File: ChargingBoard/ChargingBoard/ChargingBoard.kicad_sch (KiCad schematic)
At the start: 0 parts

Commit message: Integration
Added charging circuits to project schematic, deleted redundant schematics
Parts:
- added BT1, BT2, BT3, BT4: Battery, Battery:BatteryHolder_Keystone_1060_1x2032, symbol Device:Battery
- added C1, C11, C16, C6: 0.1u, Capacitor_SMD:C_0201_0603Metric_Pad0.64x0.40mm_HandSolder, symbol Device:C
- added C10, C15, C20, C5: 10u, symbol Device:C_Polarized
- added C12, C17, C2, C7: 33n, Capacitor_SMD:C_0201_0603Metric_Pad0.64x0.40mm_HandSolder, symbol Device:C
- added C13, C18, C3, C8: 22n, Capacitor_SMD:C_0201_0603Metric_Pad0.64x0.40mm_HandSolder, symbol Device:C
- added C14, C19, C4, C9: 10u, Capacitor_SMD:C_0201_0603Metric_Pad0.64x0.40mm_HandSolder, symbol Device:C
- added D1, D14, D19, D9: GRN, LED_SMD:LED_0201_0603Metric_Pad0.64x0.40mm_HandSolder, symbol Device:LED
- added D10, D15, D20, D5: 6V, Diode_THT:D_DO-41_SOD81_P10.16mm_Horizontal, symbol Diode:1N47xxA
- added D11, D16, D3, D6: BLU, LED_SMD:LED_0201_0603Metric_Pad0.64x0.40mm_HandSolder, symbol Device:LED
- added D12, D17, D2, D7: YEL, LED_SMD:LED_0201_0603Metric_Pad0.64x0.40mm_HandSolder, symbol Device:LED
- added D13, D18, D4, D8: RED, LED_SMD:LED_0201_0603Metric_Pad0.64x0.40mm_HandSolder, symbol Device:LED
- added L1, L2, L3, L4: 6.8u, Inductor_SMD:L_0201_0603Metric_Pad0.64x0.40mm_HandSolder, symbol Device:L
- added Q1, Q10, Q11, Q13, Q14, Q15, Q2, Q3, Q5, Q6, Q7, Q9: FQP27P06, Package_TO_SOT_THT:TO-220-3_Vertical, symbol Transistor_FET:FQP27P06
- added Q12, Q16, Q4, Q8: IRLZ44N, Package_TO_SOT_THT:TO-220-3_Vertical, symbol Transistor_FET:IRLZ44N
- added R1, R20, R21, R33, R34, R46, R47, R7: 10k, Resistor_SMD:R_0201_0603Metric_Pad0.64x0.40mm_HandSolder, symbol Device:R
- added R10, R26, R39, R52: 9.76k, Resistor_SMD:R_0201_0603Metric_Pad0.64x0.40mm_HandSolder, symbol Device:R
- added R11, R19, R32, R45: 100k, Resistor_SMD:R_0201_0603Metric_Pad0.64x0.40mm_HandSolder, symbol Device:R
- added R12, R24, R37, R50: 51k, Resistor_SMD:R_0201_0603Metric_Pad0.64x0.40mm_HandSolder, symbol Device:R
- added R13, R23, R36, R49: 100m, Resistor_SMD:R_0201_0603Metric_Pad0.64x0.40mm_HandSolder, symbol Device:R
- added R14, R15, R17, R18, R27, R28, R3, R30, R31, R4, R40, R41, R43, R44, R5, R6: 3k, Resistor_SMD:R_0201_0603Metric_Pad0.64x0.40mm_HandSolder, symbol Device:R
- added R16, R29, R42, R8: 20k, Resistor_SMD:R_0201_0603Metric_Pad0.64x0.40mm_HandSolder, symbol Device:R
- added R2, R22: 150k, Resistor_SMD:R_0201_0603Metric_Pad0.64x0.40mm_HandSolder, symbol Device:R
- added R25, R38, R51, R9: 28k, Resistor_SMD:R_0201_0603Metric_Pad0.64x0.40mm_HandSolder, symbol Device:R
- added R35, R48: 70k, Resistor_SMD:R_0201_0603Metric_Pad0.64x0.40mm_HandSolder, symbol Device:R
- added TH1, TH2, TH3, TH4: 10k, Resistor_SMD:R_0508_1220Metric_Pad1.12x2.15mm_HandSolder, symbol Device:Thermistor_NTC
- added U1, U2, U4, U5: LTC4011CFE, Package_SO:HTSSOP-20-1EP_4.4x6.5mm_P0.65mm_EP2.74x3.86mm, symbol Battery_Management:LTC4011CFE
- added U3: ATmega328-P, Package_DIP:DIP-28_W7.62mm, symbol MCU_Microchip_ATmega:ATmega328-P
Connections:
- new net: R1.1, U1.9 (V_{CDIV})
- new net: C2.1, R1.2, R2.2, U1.8 (V_{CELL})
- new net: D20.2 (A), Q14.1 (G), R47.1
- new net: R10.2, R12.2, R9.1, TH1.1
- new net: D13.1 (K), U4.2 (~{FAULT})
- new net: D13.2 (A), R30.2
- new net: R45.2, U5.10 (TIMER)
- new net: D10.2 (A), Q6.1 (G), R21.1
- new net: R24.2, R25.1, R26.2, TH2.1
- new net: R37.2, R38.1, R39.2, TH3.1
- new net: C6.1, U2.14 (INTVDD)
- new net: C7.1, R20.2, R22.2, U2.8 (V_{CELL})
- new net: R19.2, U2.10 (TIMER)
- new net: D15.2 (A), Q10.1 (G), R34.1
- new net: C1.1, U1.14 (INTVDD)
- new net: R50.2, R51.1, R52.2, TH4.1
- new net: C12.1, R33.2, R35.2, U4.8 (V_{CELL})
- new net: D12.2 (A), R28.2
- new net: D6.2 (A), R14.2
- new net: D11.2 (A), R27.2
- new net: D14.2 (A), R31.2
- new net: R32.2, U4.10 (TIMER)
- new net: L3.2, R36.1, U4.11 (SENSE)
- new net: D12.1 (K), U4.13 (~{TOC})
- new net: C11.1, U4.14 (INTVDD)
- new net: D14.1 (K), U4.19 (~{READY})
- new net: D11.1 (K), U4.3 (~{CHRG})
- new net: R33.1, U4.9 (V_{CDIV})
- new net: D18.2 (A), R43.2
- new net: D1.1 (K), U1.19 (~{READY})
- new net: D1.2 (A), R3.2
- new net: R11.2, U1.10 (TIMER)
- new net: L1.2, R13.1, U1.11 (SENSE)
- new net: D7.2 (A), R15.2
- new net: C17.1, R46.2, R48.2, U5.8 (V_{CELL})
- new net: R20.1, U2.9 (V_{CDIV})
- new net: D8.1 (K), U2.2 (~{FAULT})
- new net: D8.2 (A), R17.2
- new net: D4.2 (A), R6.2
- new net: D4.1 (K), U1.2 (~{FAULT})
- new net: C16.1, U5.14 (INTVDD)
- new net: L4.2, R49.1, U5.11 (SENSE)
- new net: D6.1 (K), U2.3 (~{CHRG})
- new net: U3.22 (GND), U3.8 (GND)
- new net: D16.2 (A), R40.2
- new net: D3.2 (A), R5.2
- new net: D2.2 (A), R4.2
- new net: D5.2 (A), Q2.1 (G), R7.1
- new net: D3.1 (K), U1.3 (~{CHRG})
- new net: D9.1 (K), U2.19 (~{READY})
- new net: D9.2 (A), R18.2
- new net: L2.2, R23.1, U2.11 (SENSE)
- new net: D17.2 (A), R41.2
- new net: D17.1 (K), U5.13 (~{TOC})
- new net: D7.1 (K), U2.13 (~{TOC})
- new net: D19.1 (K), U5.19 (~{READY})
- new net: D18.1 (K), U5.2 (~{FAULT})
- new net: D16.1 (K), U5.3 (~{CHRG})
- new net: R46.1, U5.9 (V_{CDIV})
- new net: D19.2 (A), R44.2
- new net: D2.1 (K), U1.13 (~{TOC})
- new net +12V: Q13.3 (S), Q5.3 (S)
- new net +18V: C15.1, C20.1, D15.1 (K), D20.1 (K), Q10.3 (S), Q11.3 (S), Q13.2 (D), Q14.3 (S), Q15.3 (S), Q9.2 (D), Q9.3 (S), R27.1, R28.1, R29.2, R30.1, R31.1, R34.2, R40.1, R41.1, R42.2, R43.1, R44.1, R47.2, U4.1 (DCIN), U4.18 (V_{CC}), U5.1 (DCIN), U5.18 (V_{CC})
- new net +34V: C10.1, C5.1, D10.1 (K), D5.1 (K), Q1.2 (D), Q1.3 (S), Q2.3 (S), Q3.3 (S), Q5.2 (D), Q6.3 (S), Q7.3 (S), R14.1, R15.1, R16.2, R17.1, R18.1, R21.2, R3.1, R4.1, R5.1, R6.1, R7.2, R8.2, U1.1 (DCIN), U1.18 (V_{CC}), U2.1 (DCIN), U2.18 (V_{CC})
- new net BAT1: BT1.1 (+), C4.1, Q2.2 (D), R13.2, R2.1, R48.1, U1.12 (BAT), U5.12 (BAT)
- new net BAT2: BT2.1 (+), C9.1, Q6.2 (D), R22.1, R23.2, U2.12 (BAT)
- new net BAT3: BT3.1 (+), C14.1, Q10.2 (D), R35.1, R36.2, U4.12 (BAT)
- new net BAT4: BT4.1 (+), C19.1, Q14.2 (D), R49.2
- new net BGATE1: Q4.1 (G), U1.15 (BGATE)
- new net BGATE2: Q8.1 (G), U2.15 (BGATE)
- new net BGATE3: Q12.1 (G), U4.15 (BGATE)
- new net BGATE4: Q16.1 (G), U5.15 (BGATE)
- new net GND: BT1.2 (-), BT2.2 (-), BT3.2 (-), BT4.2 (-), C1.2, C10.2, C11.2, C12.2, C13.2, C14.2, C15.2, C16.2, C17.2, C18.2, C19.2, C2.2, C20.2, C3.2, C4.2, C5.2, C6.2, C7.2, C8.2, C9.2, Q12.3 (S), Q16.3 (S), Q4.3 (S), Q8.3 (S), R11.1, R16.1, R19.1, R25.2, R29.1, R32.1, R38.2, R42.1, R45.1, R51.2, R8.1, R9.2, TH1.2, TH2.2, TH3.2, TH4.2, U1.16 (PGND), U1.21 (GND), U1.4 (CHEM), U1.5 (GND), U2.16 (PGND), U2.21 (GND), U2.4 (CHEM), U2.5 (GND), U4.16 (PGND), U4.21 (GND), U4.4 (CHEM), U4.5 (GND), U5.16 (PGND), U5.21 (GND), U5.4 (CHEM), U5.5 (GND)
- new net INFET1: Q1.1 (G), U1.20 (INFET)
- new net INFET2: Q5.1 (G), U2.20 (INFET)
- new net INFET3: Q9.1 (G), U4.20 (INFET)
- new net INFET4: Q13.1 (G), U5.20 (INFET)
- new net L1: L1.1, Q3.2 (D), Q4.2 (D)
- new net L2: L2.1, Q7.2 (D), Q8.2 (D)
- new net L3: L3.1, Q11.2 (D), Q12.2 (D)
- new net L4: L4.1, Q15.2 (D), Q16.2 (D)
- new net TGATE1: Q3.1 (G), U1.17 (TGATE)
- new net TGATE2: Q7.1 (G), U2.17 (TGATE)
- new net TGATE3: Q11.1 (G), U4.17 (TGATE)
- new net TGATE4: Q15.1 (G), U5.17 (TGATE)
- new net VRT1: R10.1, U1.6 (V_{RT})
- new net VRT2: R26.1, U2.6 (V_{RT})
- new net VRT3: R39.1, U4.6 (V_{RT})
- new net VRT4: R52.1, U5.6 (V_{RT})
- new net VTEMP1: C3.1, R12.1, U1.7 (V_{TEMP})
- new net VTEMP2: C8.1, R24.1, U2.7 (V_{TEMP})
- new net VTEMP3: C13.1, R37.1, U4.7 (V_{TEMP})
- new net VTEMP4: C18.1, R50.1, U5.7 (V_{TEMP})
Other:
- note added: "MOTOR_1"
- note added: "MOTOR_2"
- note added: "PCB_1"
- note added: "PCB_2"
- company: (none) -> Aurelia
- title: (none) -> MUSTV UOP Charging Board

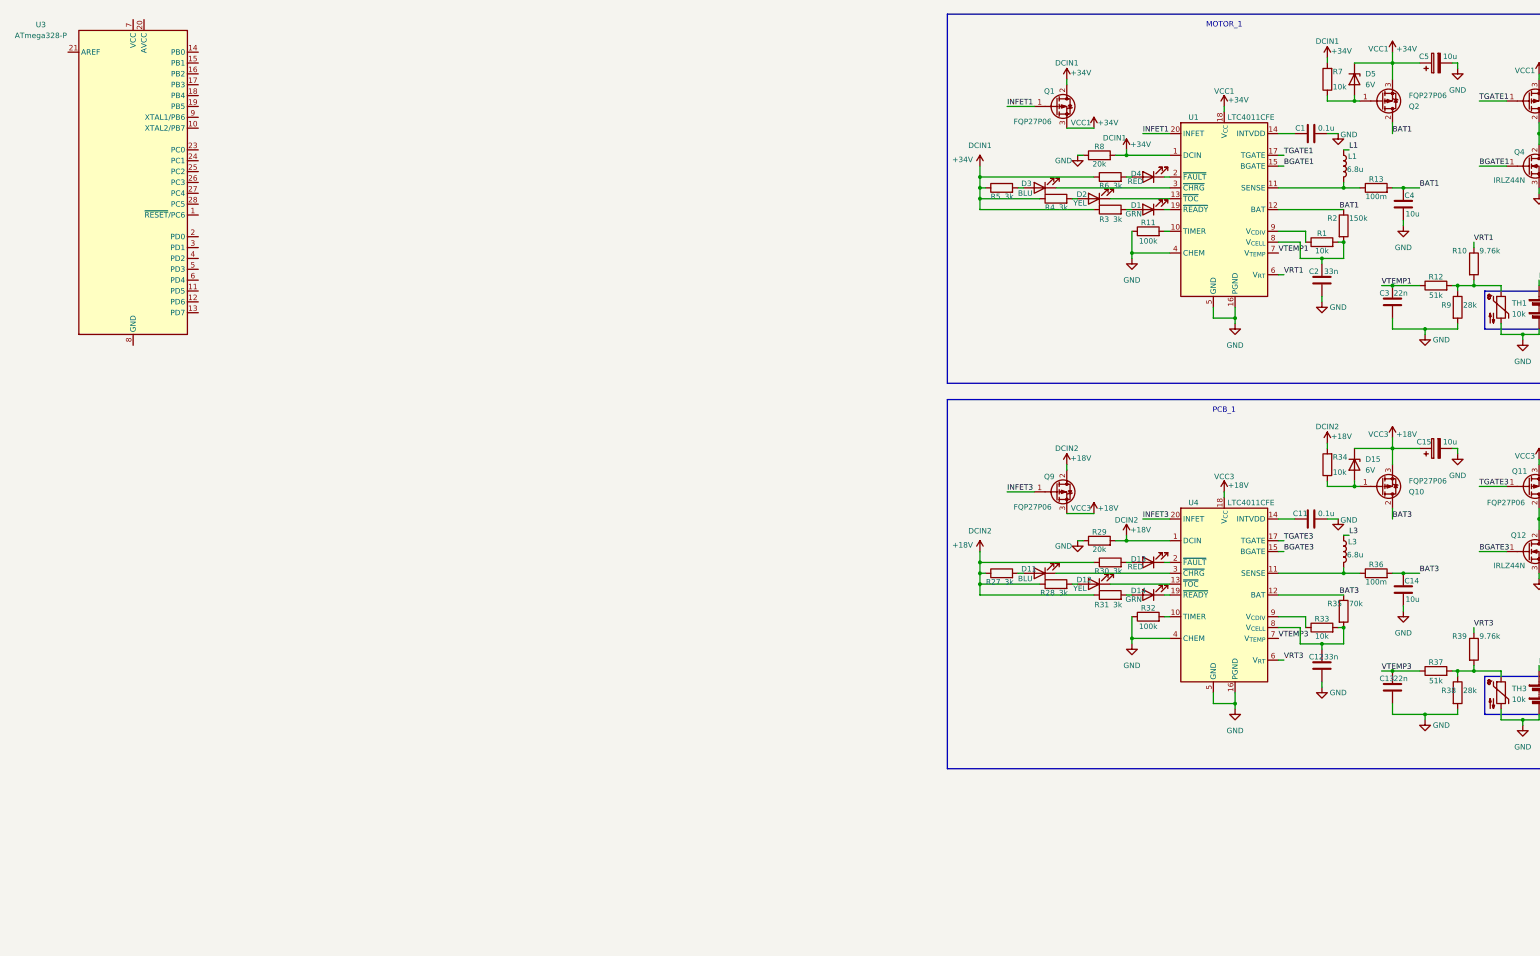
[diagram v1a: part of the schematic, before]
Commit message: SD Card and Voltage Conversion
Swapped out microcontroller, added SD card circuit and conversion terminals for voltages, added 5V to 3.3V regulator
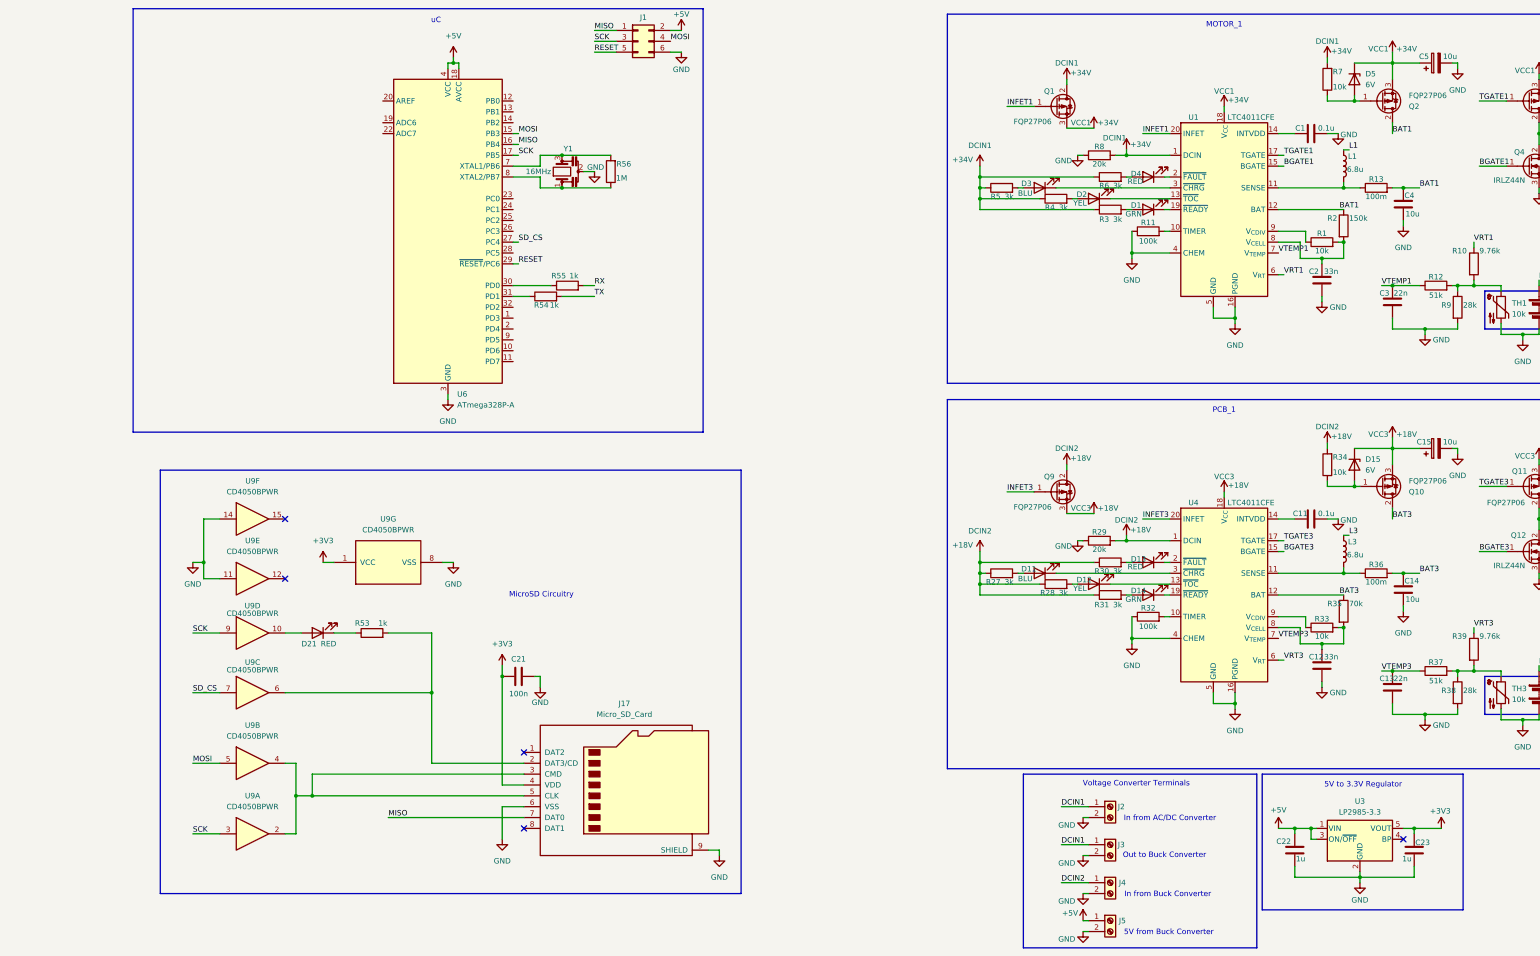
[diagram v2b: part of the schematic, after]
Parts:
- removed U3: ATmega328-P, Package_DIP:DIP-28_W7.62mm, symbol MCU_Microchip_ATmega:ATmega328-P
- added C21: 100n, Capacitor_SMD:C_0603_1608Metric_Pad1.08x0.95mm_HandSolder, symbol Device:C
- added C22, C23: 1u, Capacitor_SMD:C_0603_1608Metric_Pad1.08x0.95mm_HandSolder, symbol Device:C
- added D21: RED, LED_SMD:LED_0603_1608Metric_Pad1.05x0.95mm_HandSolder, symbol Device:LED
- added J1: Conn_02x03_Odd_Even, symbol Connector_Generic:Conn_02x03_Odd_Even
- added J17: Micro_SD_Card, Connector_Card:microSD_HC_Hirose_DM3BT-DSF-PEJS, symbol Connector:Micro_SD_Card
- added J2, J3, J4, J5: Screw_Terminal_01x02, symbol Connector:Screw_Terminal_01x02
- added R53: 1k, Resistor_SMD:R_0603_1608Metric_Pad0.98x0.95mm_HandSolder, symbol Device:R
- added R54, R55: 1k, symbol Device:R
- added R56: 1M, symbol Device:R
- added U3: LP2985-3.3, Package_TO_SOT_SMD:SOT-23-5_HandSoldering, symbol Regulator_Linear:LP2985-3.3
- added U6: ATmega328P-A, Package_QFP:TQFP-32_7x7mm_P0.8mm, symbol MCU_Microchip_ATmega:ATmega328P-A
- added U9: CD4050BPWR, Package_SO:SOIC-16_3.9x9.9mm_P1.27mm, symbol 4xxx:4050
- added Y1: 16MHz, symbol Device:Resonator
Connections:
- net GND: now also C21.2, C22.2, C23.2, J1.6 (Pin_6), J17.6 (VSS), J17.9 (SHIELD), J2.2 (Pin_2), J3.2 (Pin_2), J4.2 (Pin_2), J5.2 (Pin_2), U3.2 (GND), U6.21 (GND), U6.3 (GND), U6.5 (GND), U9.11, U9.14, U9.8 (VSS), Y1.2
- new net: R56.1, U6.8 (XTAL2/PB7), Y1.1
- new net: R56.2, U6.7 (XTAL1/PB6), Y1.3
- new net: J17.3 (CMD), J17.5 (CLK), U9.2, U9.4
- new net: D21.1 (K), R53.1
- new net: J17.2 (DAT3/CD), R53.2, U9.6
- new net: D21.2 (A), U9.10
- new net: R55.1, U6.30 (PD0)
- new net: R54.1, U6.31 (PD1)
- new net +3V3: C21.1, C23.1, J17.4 (VDD), U3.5 (VOUT), U9.1 (VCC)
- new net +5V: C22.1, J1.2 (Pin_2), J5.1 (Pin_1), U3.1 (VIN), U3.3 (ON/~{OFF}), U6.18 (AVCC), U6.4 (VCC), U6.6 (VCC)
- new net DCIN1: J2.1 (Pin_1), J3.1 (Pin_1)
- new net DCIN2: J4.1 (Pin_1)
- new net MISO: J1.1 (Pin_1), J17.7 (DAT0), U6.16 (PB4)
- new net MOSI: J1.4 (Pin_4), U6.15 (PB3), U9.5
- new net RESET: J1.5 (Pin_5), U6.29 (~{RESET}/PC6)
- new net RX: R55.2
- new net SCK: J1.3 (Pin_3), U6.17 (PB5), U9.3, U9.9
- new net SD_CS: U6.27 (PC4), U9.7
- new net TX: R54.2
- no-connect marks 0 -> 5
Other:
- note added: "5V from Buck Converter"
- note added: "5V to 3.3V Regulator"
- note added: "In from AC/DC Converter"
- note added: "In from Buck Converter"
- note added: "MicroSD Circuitry"
- note added: "Out to Buck Converter"
- note added: "Voltage Converter Terminals"
- note added: "uC"
